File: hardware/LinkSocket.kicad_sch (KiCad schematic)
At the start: 4 parts, among them J401 2x05_Horizontal, U401 THVD24x2

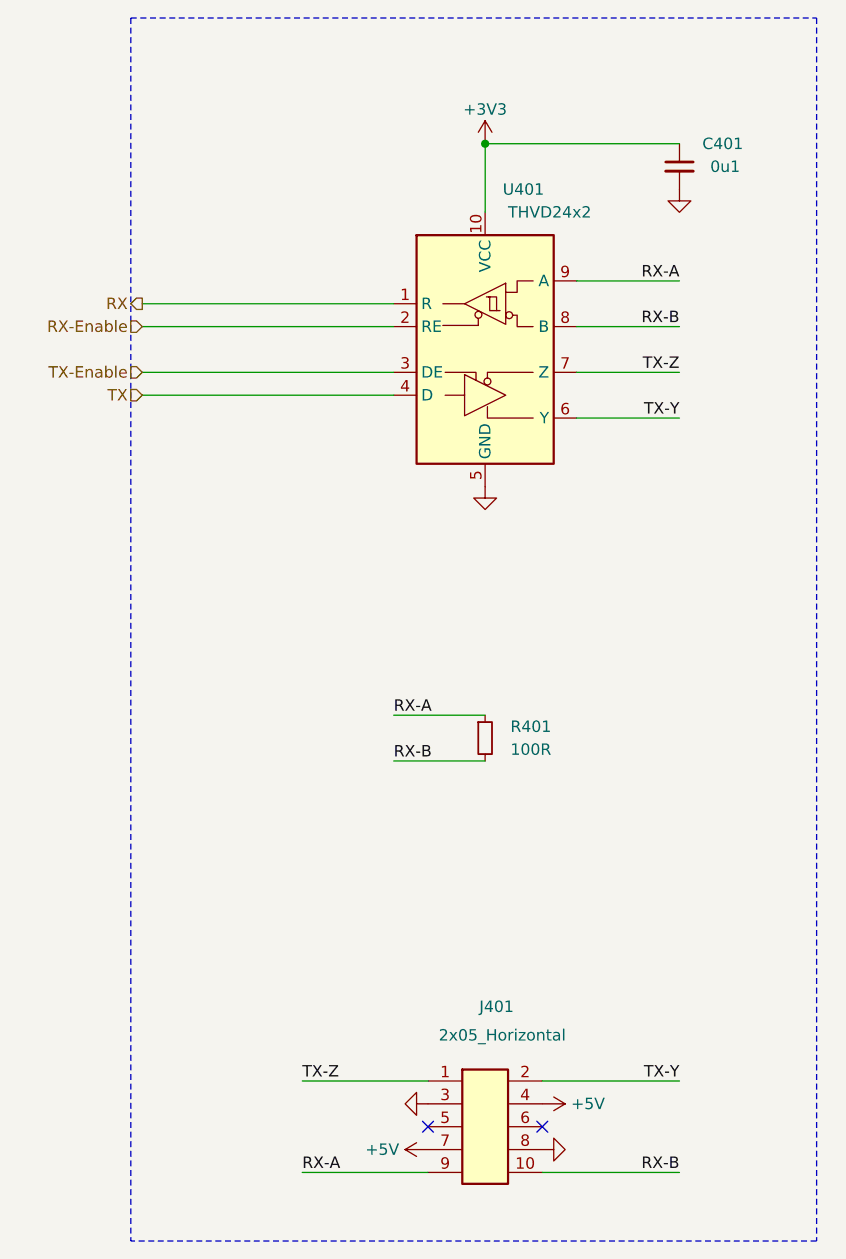
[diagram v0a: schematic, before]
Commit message: Replace Order_Number
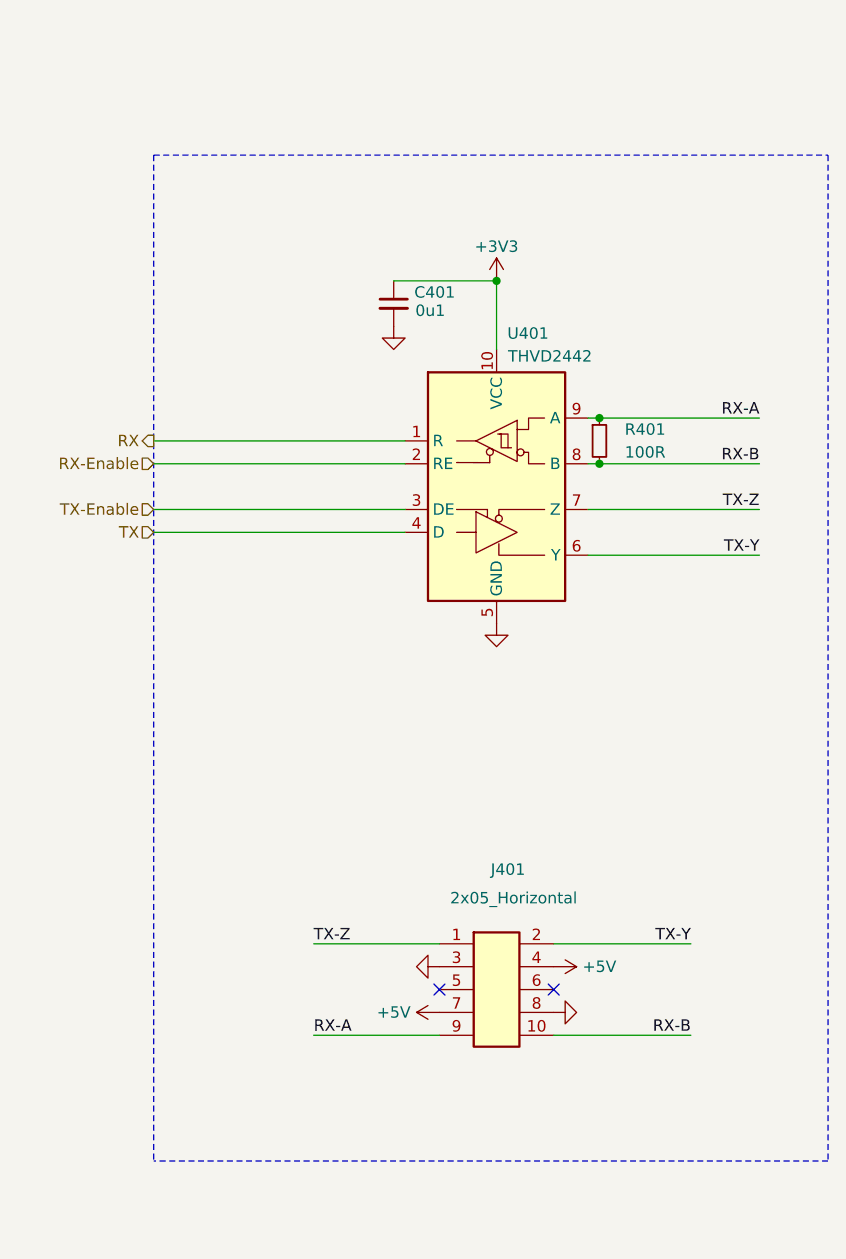
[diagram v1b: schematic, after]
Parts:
- C401: footprint Capacitor_SMD:C_0603_1608Metric -> V2_Capacitor_SMD:C_0603; symbol Device:C_Small -> V2_Device:C_0603_0u1; Manufacturer (none) -> TDK; Mouser (none) -> 810-CGA3E2X7R1H104MA; Product (none) -> CGA3E2X7R1H104M080AA; Rating (none) -> 50V
- J401: Manufacturer (none) -> Amphenol FCI; Mouser (none) -> 649-200211120001T4LF; Product (none) -> 20021112-00010T4LF
- R401: footprint Resistor_SMD:R_0603_1608Metric -> V2_Resistor_SMD:R_0603; symbol Device:R_Small -> V2_Device:R_0603_100R; Manufacturer (none) -> Vishay; Mouser (none) -> 71-CRCW0603100RFKEAH; Product (none) -> CRCW0603100RFKEAHP; Rating (none) -> 330mW
- U401: value THVD24x2 -> THVD2442; symbol V2_Interface_RS485:THVD24x2 -> V2_Interface_RS485:THVD2442; Manufacturer (none) -> Texas Instruments; Mouser (none) -> 595-THVD2442DRCR; Product (none) -> THVD2442DRCR
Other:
- moved on the sheet: C401, J401, R401, U401

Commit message: Update Library
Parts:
- C401: symbol V2_Device:C_0603_0u1 -> V2_Capacitor:0603_0u1
- R401: symbol V2_Device:R_0603_100R -> V2_Resistor:0603_100R
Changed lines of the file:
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@@
 		(on_board yes)
 		(dnp no)
-		(property "Reference" "#PWR0403"
+		(property "Reference" "#PWR403"
 			(at 153.67 68.58 0)
 			(effects
@@
 			(project "wave"
 				(path "/6c8448b4-b04d-47e1-934e-e40cbe27a7be/2a03ea79-269e-4abf-833c-000ba0ff13d7"
-					(reference "#PWR0403")
+					(reference "#PWR403")
 					(unit 1)
 				)
@@
 		(on_board yes)
 		(dnp no)
-		(property "Reference" "#PWR0401"
+		(property "Reference" "#PWR401"
 			(at 140.97 140.97 0)
 			(effects
@@
 			(project "wave"
 				(path "/6c8448b4-b04d-47e1-934e-e40cbe27a7be/2a03ea79-269e-4abf-833c-000ba0ff13d7"
-					(reference "#PWR0401")
+					(reference "#PWR401")
 					(unit 1)
 				)
@@
 		(on_board yes)
 		(dnp no)
-		(property "Reference" "#PWR0404"
+		(property "Reference" "#PWR404"
 			(at 153.67 109.22 0)
 			(effects
@@
 			(project "wave"
 				(path "/6c8448b4-b04d-47e1-934e-e40cbe27a7be/2a03ea79-269e-4abf-833c-000ba0ff13d7"
-					(reference "#PWR0404")
+					(reference "#PWR404")
 					(unit 1)
 				)
@@
 		(on_board yes)
 		(dnp no)
-		(property "Reference" "#PWR0407"
+		(property "Reference" "#PWR407"
 			(at 142.24 76.2 0)
 			(effects
@@
 			(project "wave"
 				(path "/6c8448b4-b04d-47e1-934e-e40cbe27a7be/2a03ea79-269e-4abf-833c-000ba0ff13d7"
-					(reference "#PWR0407")
-					(unit 1)
-				)
-			)
-		)
-	)
-	(symbol
-		(lib_id "V2_Device:R_0603_100R")
+					(reference "#PWR407")
+					(unit 1)
+				)
+			)
+		)
+	)
+	(symbol
+		(lib_id "V2_Resistor:0603_100R")
 		(at 165.1 82.55 0)
 		(unit 1)
@@
 		(on_board yes)
 		(dnp no)
-		(property "Reference" "#PWR0406"
+		(property "Reference" "#PWR406"
 			(at 166.37 146.05 0)
 			(effects
@@
 			(project "wave"
 				(path "/6c8448b4-b04d-47e1-934e-e40cbe27a7be/2a03ea79-269e-4abf-833c-000ba0ff13d7"
-					(reference "#PWR0406")
+					(reference "#PWR406")
 					(unit 1)
 				)
@@
 	)
 	(symbol
-		(lib_id "V2_Device:C_0603_0u1")
+		(lib_id "V2_Capacitor:0603_0u1")
 		(at 142.24 67.31 0)
 		(unit 1)
@@
 		(on_board yes)
 		(dnp no)
-		(property "Reference" "#PWR0402"
+		(property "Reference" "#PWR402"
 			(at 151.13 146.05 0)
 			(effects
@@
 			(project "wave"
 				(path "/6c8448b4-b04d-47e1-934e-e40cbe27a7be/2a03ea79-269e-4abf-833c-000ba0ff13d7"
-					(reference "#PWR0402")
+					(reference "#PWR402")
 					(unit 1)
 				)
@@
 		(on_board yes)
 		(dnp no)
-		(property "Reference" "#PWR0405"
+		(property "Reference" "#PWR405"
 			(at 156.21 140.97 0)
 			(effects
@@
 			(project "wave"
 				(path "/6c8448b4-b04d-47e1-934e-e40cbe27a7be/2a03ea79-269e-4abf-833c-000ba0ff13d7"
-					(reference "#PWR0405")
-					(unit 1)
-				)
+					(reference "#PWR405")
+					(unit 1)
+				)
